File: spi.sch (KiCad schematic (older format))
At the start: 12 parts, among them U5 MS5611-01BA03, U6 MPU-6000, U7 MPU-9250

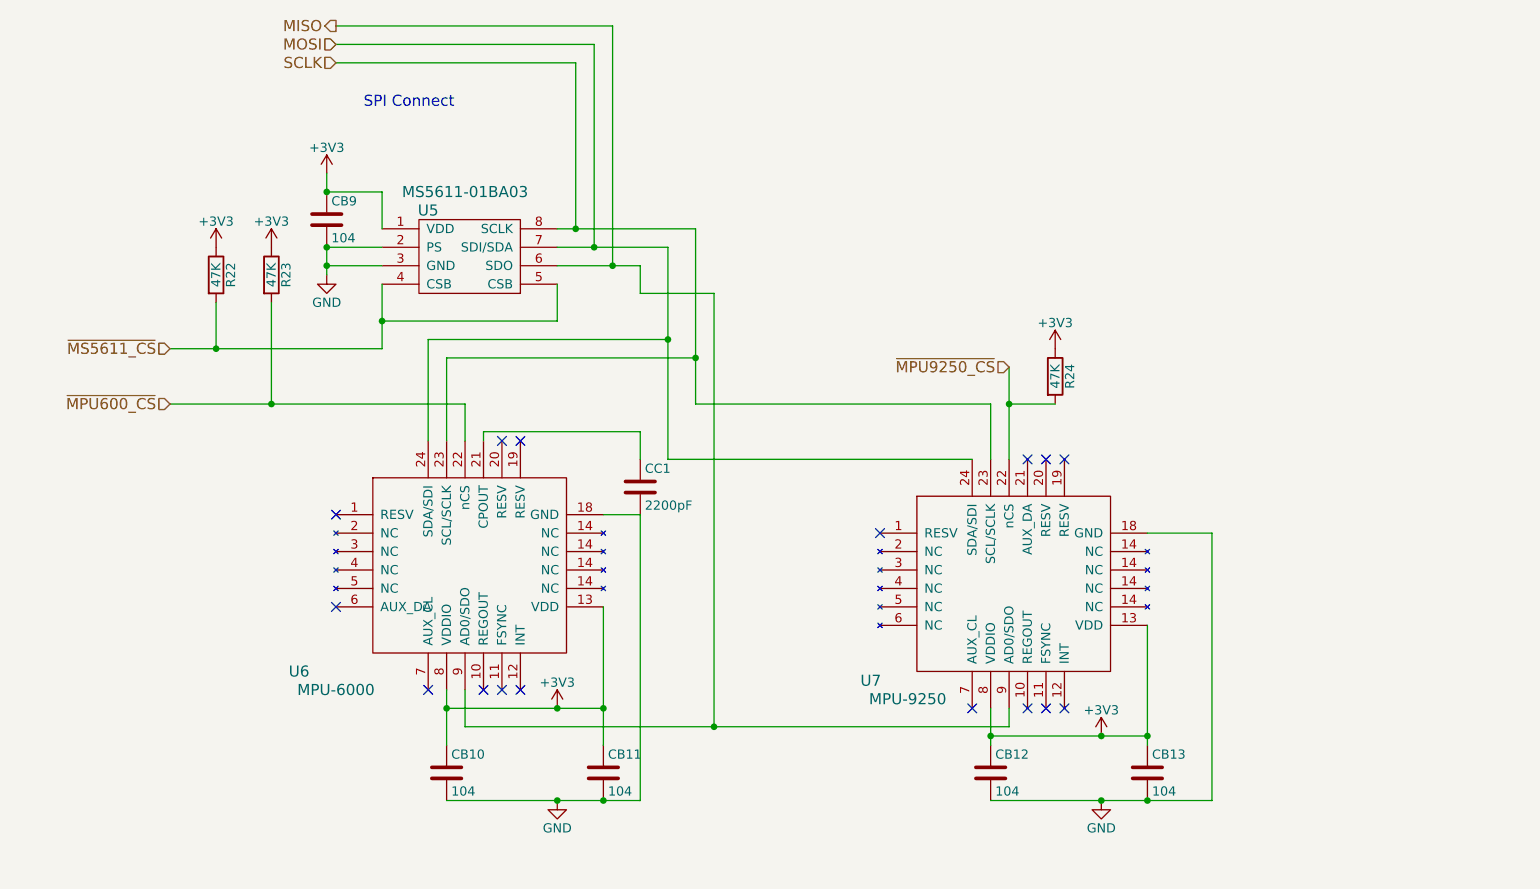
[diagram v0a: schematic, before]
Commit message: Deleted unnecessary files and splitting schmatics.
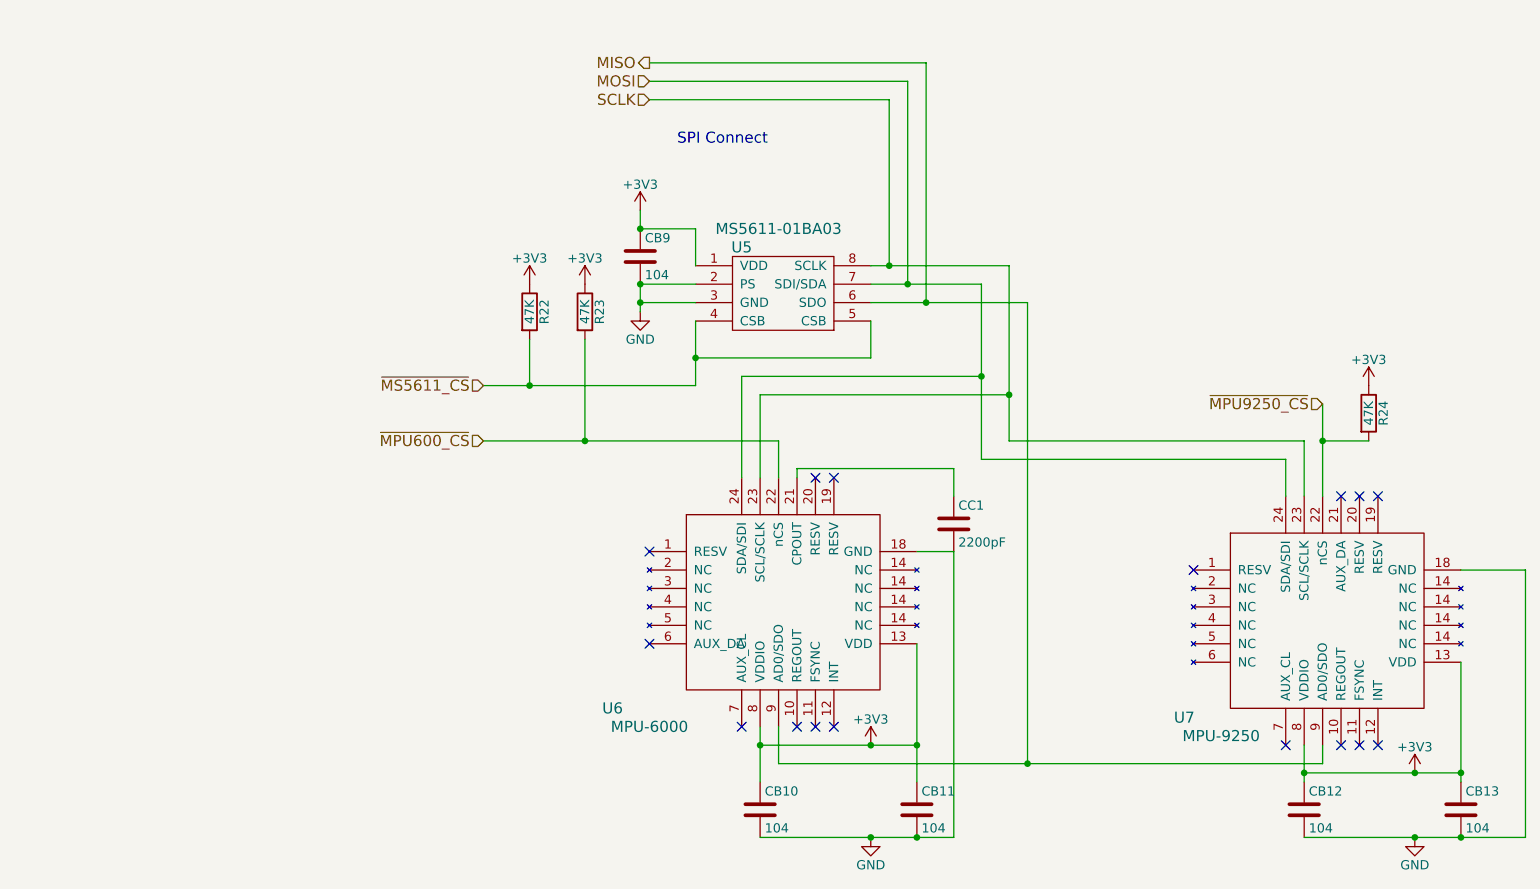
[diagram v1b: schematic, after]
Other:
- moved on the sheet: CB10, CB11, CB12, CB13, CB9, CC1, R22, R23, R24, U5, U6, U7
